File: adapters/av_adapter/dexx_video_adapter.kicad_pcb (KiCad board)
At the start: 2 copper layers, 46.9 x 49.4 mm, 6 parts, among them J1 SCART-F, J2 Pr, J3 Y, J4 Pb, J5 AudioJack3, J6 DB15_Female_HighDensity

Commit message: update av_adapter board to v1.1
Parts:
- added MH1: MountingHole, MountingHole:MountingHole_3.2mm_M3_ISO14580_Pad, F.Cu at (40.4, 64.8)
- added MH2: MountingHole, MountingHole:MountingHole_3.2mm_M3_ISO14580_Pad, F.Cu at (58.1, 16.6)
- added R1: 500, custom_components:SM0603_Resistor_libcms, F.Cu at (48.6, 48.0)
- added R2: 180, custom_components:SM0603_Resistor_libcms, F.Cu at (51.6, 47.9)
- added SW1: SW_SPDT, custom_components:SWITCH_11MA1QS1, F.Cu at (49.2, 65.6)
- J5: footprint custom_components:SJ1-3533NG -> Connector_Audio:Jack_3.5mm_CUI_SJ1-3533NG_Horizontal
- moved J6 4.00 mm to (32.7, 48.2)
- moved J5 2.00 mm to (26.5, 21.1), turned to 90 degrees
- moved J4 0.80 mm to (51.2, 25.2)
- moved J2 0.80 mm to (51.2, 55.2)
- moved J3 0.80 mm to (51.2, 40.2)
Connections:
- J1 pad 16: unconnected-(J1-Pad16) -> /AV_RGB_STATUS
- J1 pad 19: unconnected-(J1-Pad19) -> /AV_S_OUT
- J6 pad 4: /AV_S -> /AV_S_SEL
- J6 pad 9: unconnected-(J6-Pad9) -> /DDC_5V
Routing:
- net /AV_S_SEL: track 0.00 -> 34.0 mm
- net /DDC_5V: track 0.00 -> 27.4 mm, vias 0 -> 1
- net /AV_S: track 44.9 -> 18.5 mm
- net /AV_RGB_STATUS: track 0.00 -> 17.9 mm
- net /AV_S_OUT: track 0.00 -> 17.9 mm
- net /AV_VS: track 42.4 -> 48.4 mm
- net /AV_G: track 30.5 -> 35.8 mm
- net /AV_B: track 44.3 -> 48.9 mm
- net /AV_HS: track 41.9 -> 45.8 mm
- net /AV_R: track 27.5 -> 30.8 mm
- net /AV_AR: track 37.3 -> 35.8 mm
- net /AV_AL: track 47.5 -> 46.8 mm
- net GND: vias 153 -> 134
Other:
- board size 46.9 x 49.4 mm -> 46.9 x 55.2 mm
- board text added: "AV adapter v1.1 for * DExx-vd_isl * OSSC Pro"
- board text added: "|- | SCART_O | -| SCART_I"
- board text removed: "AV adapter for * DExx-vd_isl * OSSC Pro"

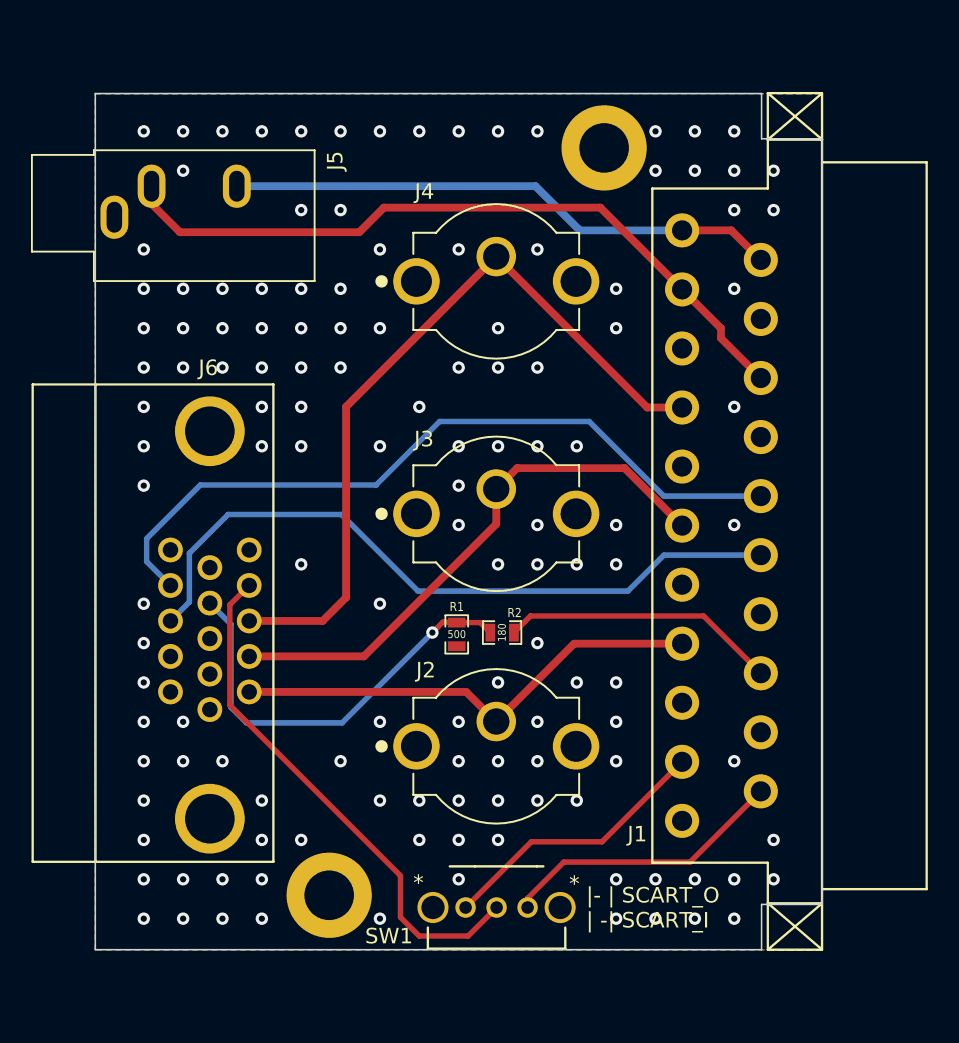
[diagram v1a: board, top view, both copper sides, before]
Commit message: update av_adapter to v1.2
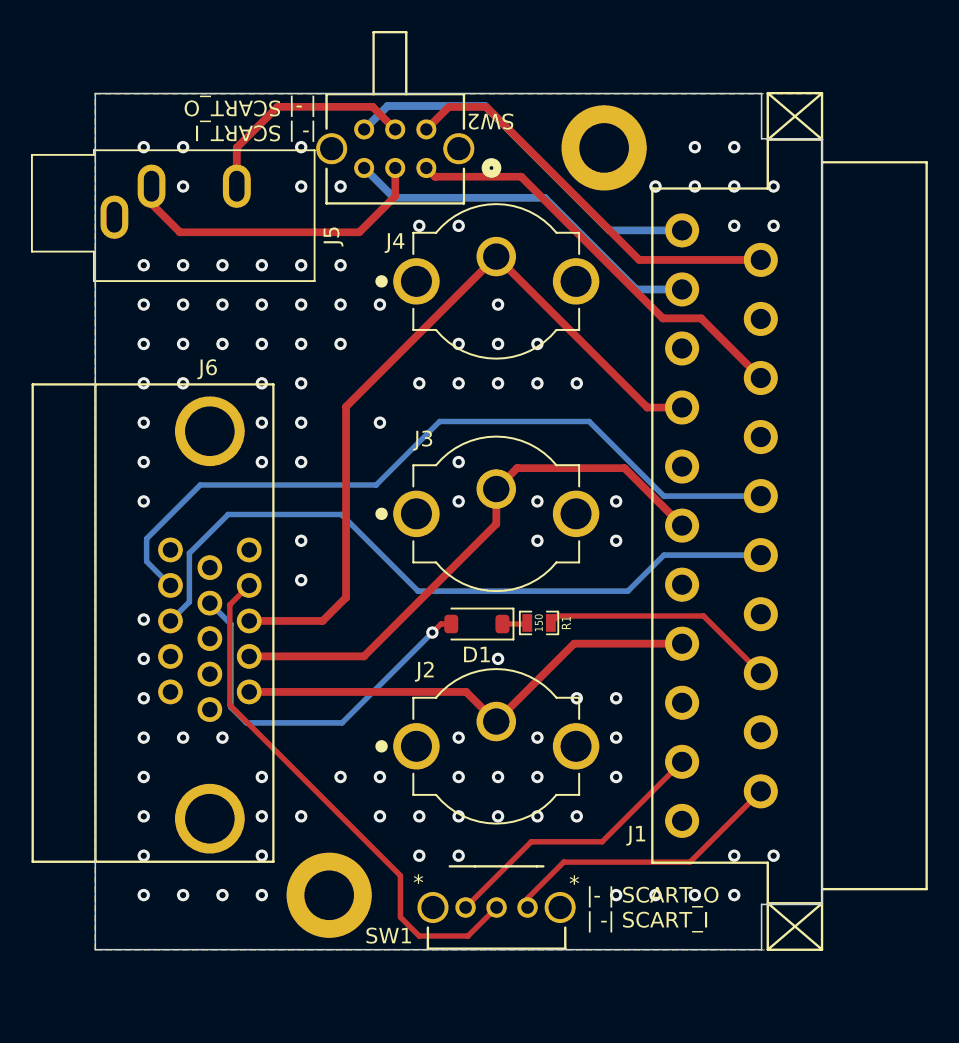
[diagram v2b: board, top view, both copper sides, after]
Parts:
- removed R2: 180, custom_components:SM0603_Resistor_libcms
- added D1: 1N4148W, Diode_SMD:D_SOD-123, F.Cu at (49.9, 47.3)
- added SW2: SW_DPDT_x2, custom_components:SW6_OS202011MA0QS1_CNK, F.Cu at (46.7, 17.9)
- R1: value 500 -> 150
- moved R1 5.36 mm to (53.9, 47.2), turned to 180 degrees
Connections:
- J1 pad 1: /AV_AR -> /AV_AR_OUT
- J1 pad 3: /AV_AL -> /AV_AL_OUT
- J5 pad R: /AV_AR -> /AV_AR_SEL
- J5 pad T: /AV_AL -> /AV_AL_SEL
- R1 pad 1: /DDC_5V -> /AV_RGB_STATUS
- R1 pad 2: GND -> Net-(D1-K)
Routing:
- net /AV_AR_OUT: track 0.00 -> 24.5 mm
- net /AV_AL_OUT: track 0.00 -> 23.8 mm
- net /AV_AL_SEL: track 0.00 -> 20.4 mm
- net /AV_AL: track 46.8 -> 27.2 mm
- net /AV_AR_SEL: track 0.00 -> 14.4 mm
- net /AV_AR: track 35.8 -> 26.3 mm
- net /DDC_5V: track 27.4 -> 24.6 mm
- net /AV_RGB_STATUS: track 17.9 -> 15.3 mm
- net Net-(D1-K): track 0.00 -> 1.63 mm
- net GND: vias 134 -> 107
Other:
- board text added: "AV adapter v1.2 for * DExx-vd_isl * OSSC Pro"
- board text added: "|- | SCART_I | -| SCART_O"
- board text removed: "AV adapter v1.1 for * DExx-vd_isl * OSSC Pro"

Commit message: update av_adapter to v1.3
* add compatibility mode for VGA cables with pin 4 missing or grounded
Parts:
- added R2: 470, custom_components:SM0603_Resistor_libcms, F.Cu at (58.7, 50.7)
- added SYM1: Logo_Open_Hardware_Small, Symbol:WEEE-Logo_4.2x6mm_SilkScreen, F.Cu at (40.5, 38.2)
- SW1: footprint custom_components:SWITCH_11MA1QS1 -> custom_components:SW6_OS202011MA0QS1_CNK
- SW2: value SW_DPDT_x2 -> SW_SPDT
- moved SW1 2.10 mm to (49.2, 63.5)
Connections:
- SW1 pad 1: /AV_S_OUT -> unconnected-(SW1-A-Pad1)
- SW1 pad 2: /AV_S_SEL -> Net-(R2-Pad1)
- SW1 pad 3: /AV_S -> /AV_S_OUT
- SW1 pad 4: (no net) -> /AV_S_OUT
- SW1 pad 5: (no net) -> /AV_S_SEL
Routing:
- net Net-(R2-Pad1): track 0.00 -> 18.8 mm
- net /AV_HS: track 45.8 -> 53.2 mm, vias 0 -> 1
- net /AV_S: track 18.5 -> 19.9 mm
- net /AV_S_OUT: track 17.9 -> 18.9 mm
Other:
- board text added: "AV adapter v1.3 for * DExx-vd_isl * OSSC Pro"
- board text removed: "AV adapter v1.2 for * DExx-vd_isl * OSSC Pro"
